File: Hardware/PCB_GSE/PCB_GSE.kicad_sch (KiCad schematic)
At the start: 37 parts, among them J1 Conn_01x06_Pin, U1 STM32F103CBT6

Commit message: wip : Done routing
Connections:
- net 12V_An: now also U1.17 (PA7); no longer U1.14 (PA4)
- net 5V_An: now also U1.18 (PB0); no longer U1.17 (PA7)
- net LCell_An: now also U1.10 (PA0); no longer U1.11 (PA1)
- net Power_Good_12V: now also U1.14 (PA4); no longer U1.15 (PA5)
- net Power_Good_5V: now also U1.15 (PA5); no longer U1.18 (PB0)
- net Pressure_An: now also U1.11 (PA1); no longer U1.10 (PA0)
- net Temp_An: now also U1.13 (PA3); no longer U1.12 (PA2)
- net Valve1_Open: now also U1.31 (PA10); no longer U1.33 (PA12)
- net Valve3_Open: now also U1.33 (PA12); no longer U1.31 (PA10)
- net Vin_An: now also U1.12 (PA2); no longer U1.13 (PA3)

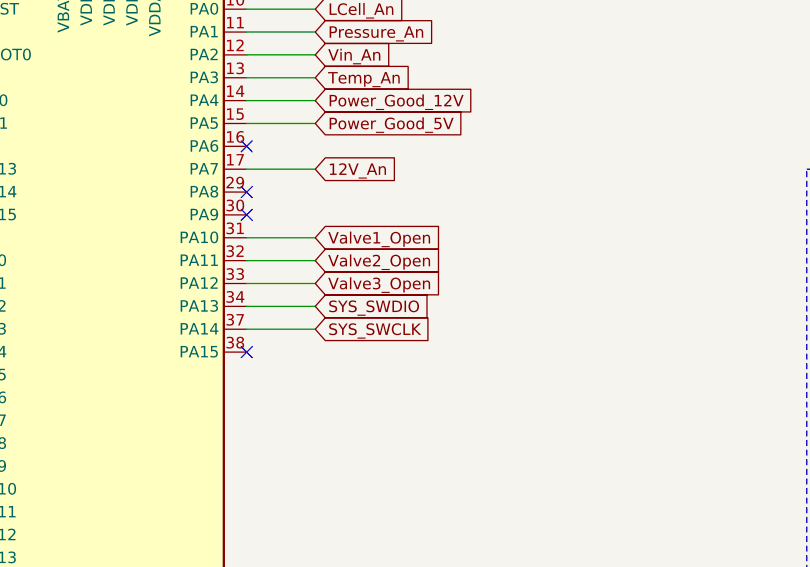
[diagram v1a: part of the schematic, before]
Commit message: fix : replace valve 3 with servomotor on schematic
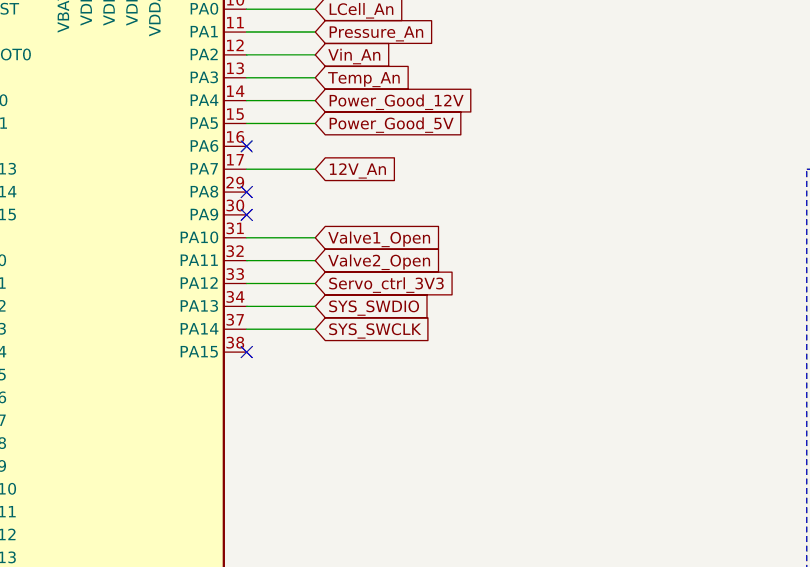
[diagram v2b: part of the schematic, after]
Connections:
- net Valve3_Open renamed Servo_ctrl_3V3
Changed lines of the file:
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@@
 		)
 	)
-	(global_label "Valve3_Open"
+	(global_label "Servo_ctrl_3V3"
 		(shape input)
 		(at 171.45 81.28 0)
@@
 		)
 		(property "Intersheetrefs" "${INTERSHEET_REFS}"
-			(at 186.2884 81.28 0)
+			(at 188.3446 81.28 0)
 			(effects
 				(font

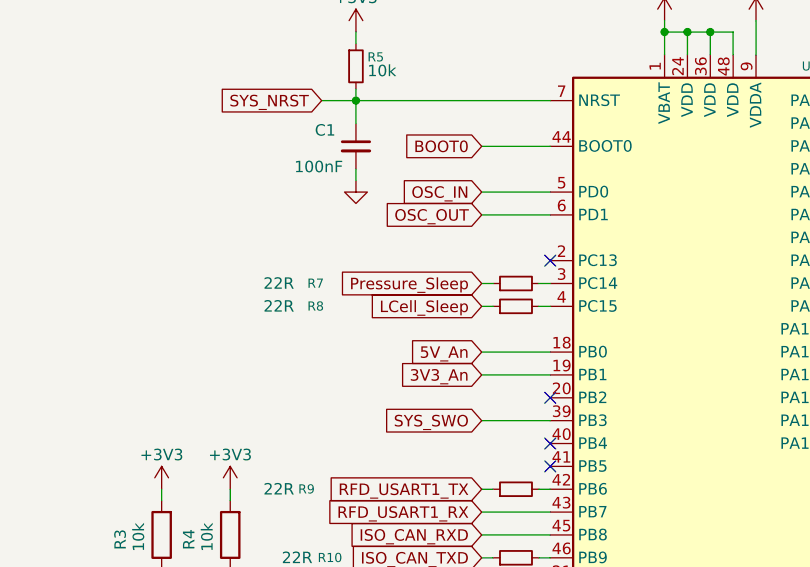
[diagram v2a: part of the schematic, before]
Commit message: fix : replace Pressure sensor amplification circuit with new voltage divider circuit
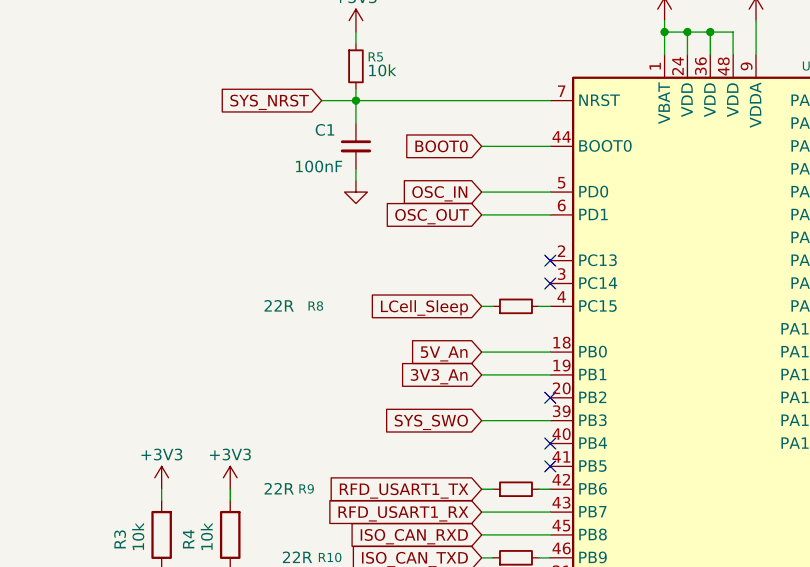
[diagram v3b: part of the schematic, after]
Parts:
- removed R7: 22R, Resistor_SMD:R_0603_1608Metric, symbol Device:R_Small
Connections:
- no-connect marks 10 -> 11
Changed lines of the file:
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@@
+	)
+	(no_connect
+		(at 130.81 71.12)
 	)
 	(no_connect
@@
 	(wire
 		(pts
-			(xy 123.19 71.12) (xy 124.46 71.12)
-		)
-		(stroke
-			(width 0)
-			(type default)
-		)
-	)
-	(wire
-		(pts
 			(xy 205.74 25.4) (xy 208.28 25.4)
 		)
@@
 	(wire
 		(pts
-			(xy 129.54 71.12) (xy 130.81 71.12)
-		)
-		(stroke
-			(width 0)
-			(type default)
-		)
-	)
-	(wire
-		(pts
 			(xy 266.7 34.29) (xy 266.7 36.83)
 		)
@@
 			(width 0)
 			(type default)
-		)
-	)
-	(global_label "Pressure_Sleep"
-		(shape input)
-		(at 123.19 71.12 180)
-		(fields_autoplaced yes)
-		(effects
-			(font
-				(size 1.27 1.27)
-			)
-			(justify right)
-		)
-		(property "Intersheetrefs" "${INTERSHEET_REFS}"
-			(at 105.8115 71.12 0)
-			(effects
-				(font
-					(size 1.27 1.27)
-				)
-				(justify right)
-				(hide yes)
-			)
 		)
 	)
@@
 					(unit 1)
 				)
-			)
-		)
-	)
-	(symbol
-		(lib_id "Device:R_Small")
-		(at 127 71.12 90)
-		(unit 1)
-		(exclude_from_sim no)
-		(in_bom yes)
-		(on_board yes)
-		(dnp no)
-		(property "Reference" "R7"
-			(at 105.664 71.12 90)
-			(effects
-				(font
-					(size 1.016 1.016)
-				)
-				(justify left)
-			)
-		)
-		(property "Value" "22R"
-			(at 102.362 71.12 90)
-			(effects
-				(font
-					(size 1.27 1.27)
-				)
-				(justify left)
-			)
-		)
-		(property "Footprint" "Resistor_SMD:R_0603_1608Metric"
-			(at 127 71.12 0)
-			(effects
-				(font
-					(size 1.27 1.27)
-				)
-				(hide yes)
-			)
-		)
-		(property "Datasheet" "https://www.digikey.ca/en/products/detail/rohm-semiconductor/ESR03EZPJ220/1983463"
-			(at 127 71.12 0)
-			(effects
-				(font
-					(size 1.27 1.27)
-				)
-				(hide yes)
-			)
-		)
-		(property "Description" "Resistor, small symbol"
-			(at 127 71.12 0)
-			(effects
-				(font
-					(size 1.27 1.27)
-				)
-				(hide yes)
-			)
-		)
-		(property "DigiKey_Part_Number" "RHM22DCT-ND"
-			(at 127 71.12 90)
-			(effects
-				(font
-					(size 1.27 1.27)
-				)
-				(hide yes)
-			)
-		)
-		(property "Manufacturer_Part_Number" "ESR03EZPJ220"
-			(at 127 71.12 90)
-			(effects
-				(font
-					(size 1.27 1.27)
-				)
-				(hide yes)
-			)
-		)
-		(pin "1"
-		)
-		(pin "2"
-		)
-		(instances
-			(project "PCB_GSE"
-				(path "/a63f9ed4-21e4-42d0-8bfc-f96143f84d4d"
-					(reference "R7")
-					(unit 1)
-				)

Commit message: fix : done silkscreen and finition
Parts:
- renumbered C2 to C13, C5 to C14, C7 to C15, C11 to C16, C10 to C18, C4 to C19, C1 to C20, C6 to C22, C9 to C24, C8 to C26, C3 to C28, LED1 to D4, FB1 to FB2, H2 to H1, H1 to H2, J1 to J4, R8 to R10, R5 to R17, R1 to R21, R2 to R22, R3 to R23, R4 to R24, R11 to R6, R10 to R7, R9 to R8, R12 to R9, U1 to U5, XTAL-1 to Y1

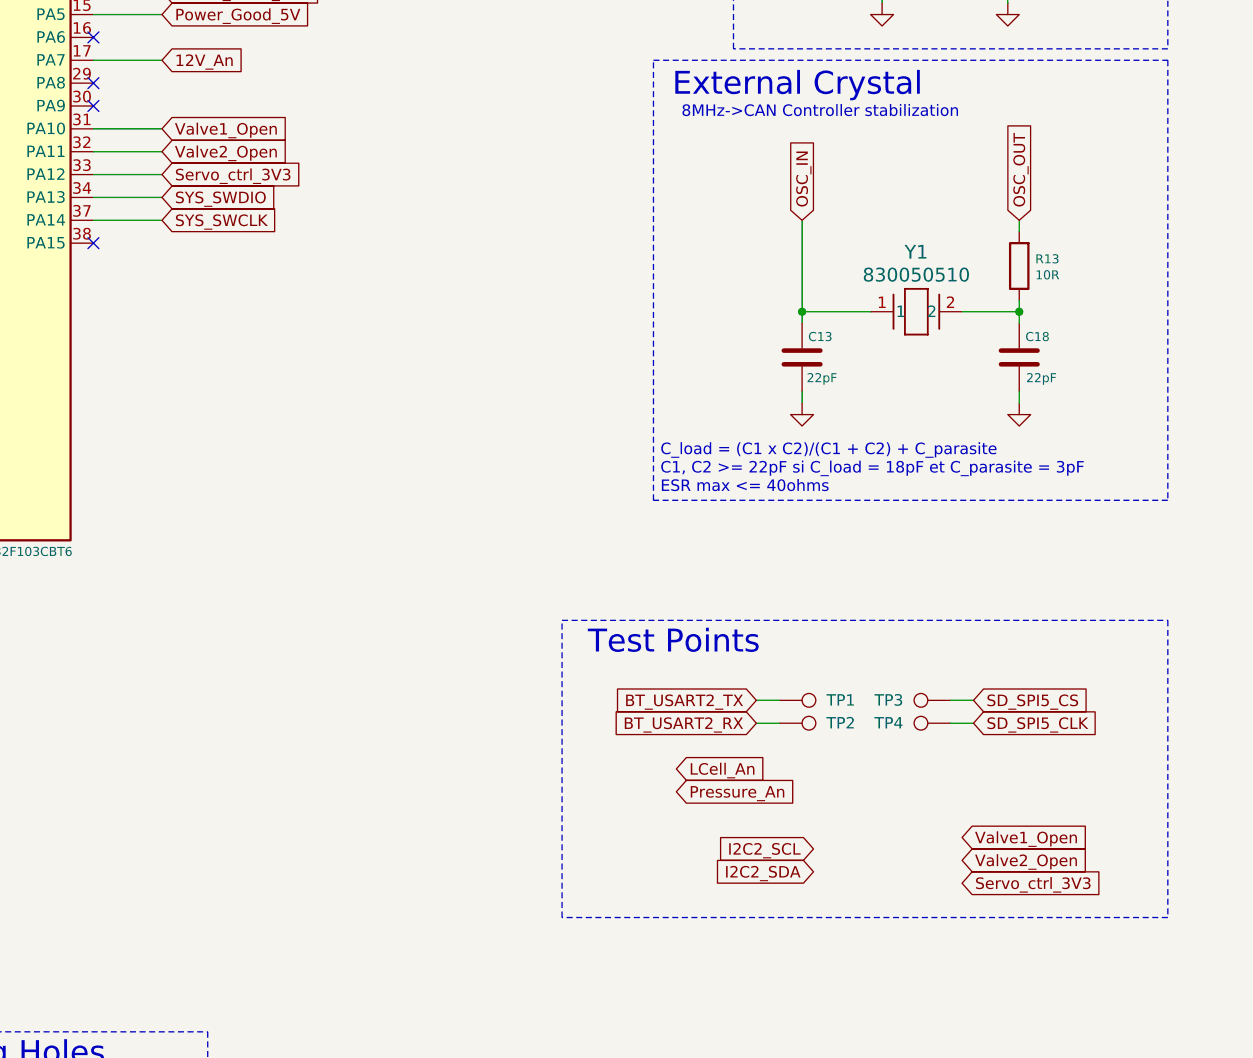
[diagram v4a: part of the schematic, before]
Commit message: fix(gse): Vin servo
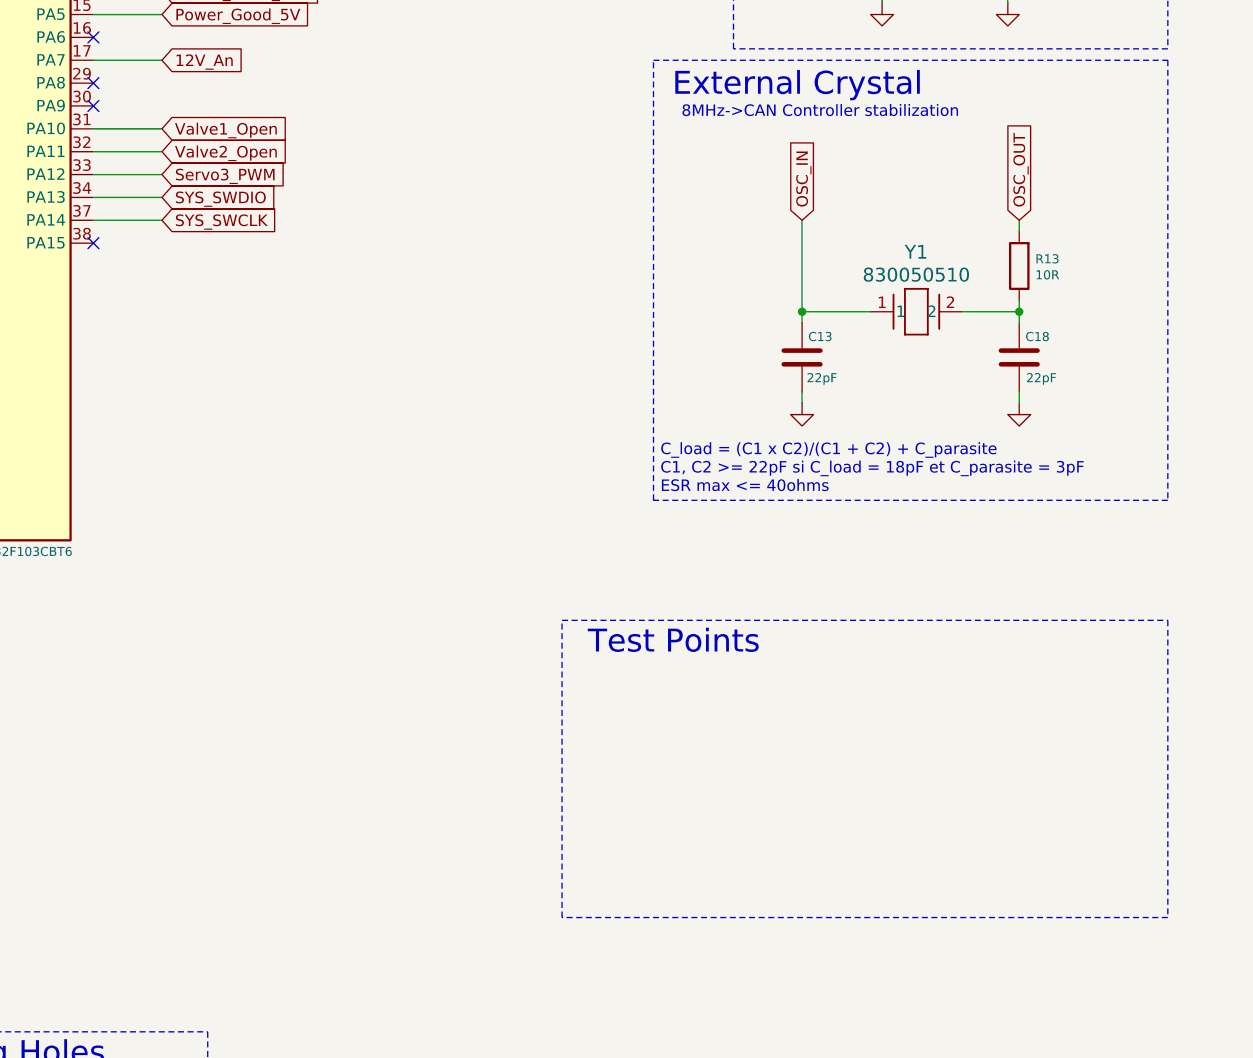
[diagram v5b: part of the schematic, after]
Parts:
- removed TP1, TP2, TP3, TP4: TestPoint, TestPoint:TestPoint_Pad_D1.0mm, symbol Connector:TestPoint
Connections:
- net Servo_ctrl_3V3 renamed Servo3_PWM

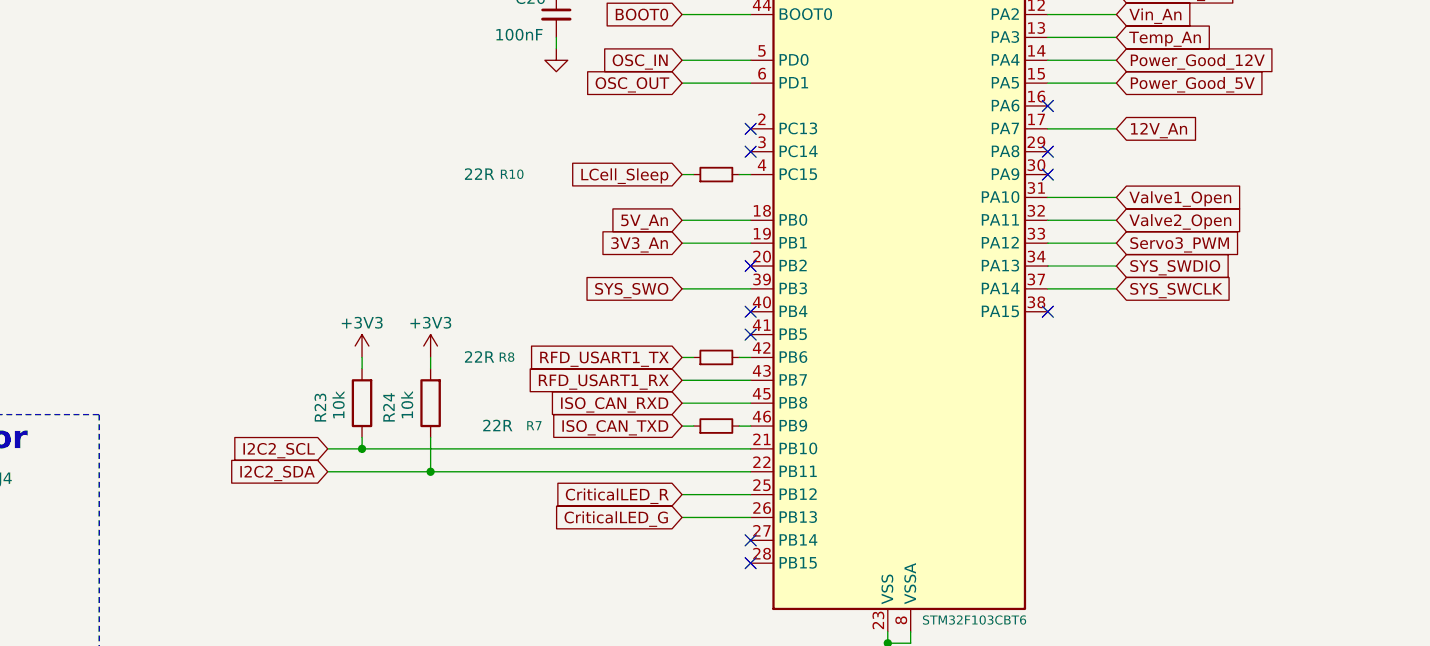
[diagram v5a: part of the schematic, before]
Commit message: fix(gse): change Servo3_PWM -> TIM1_CH2, change Valve1/2_Open pin
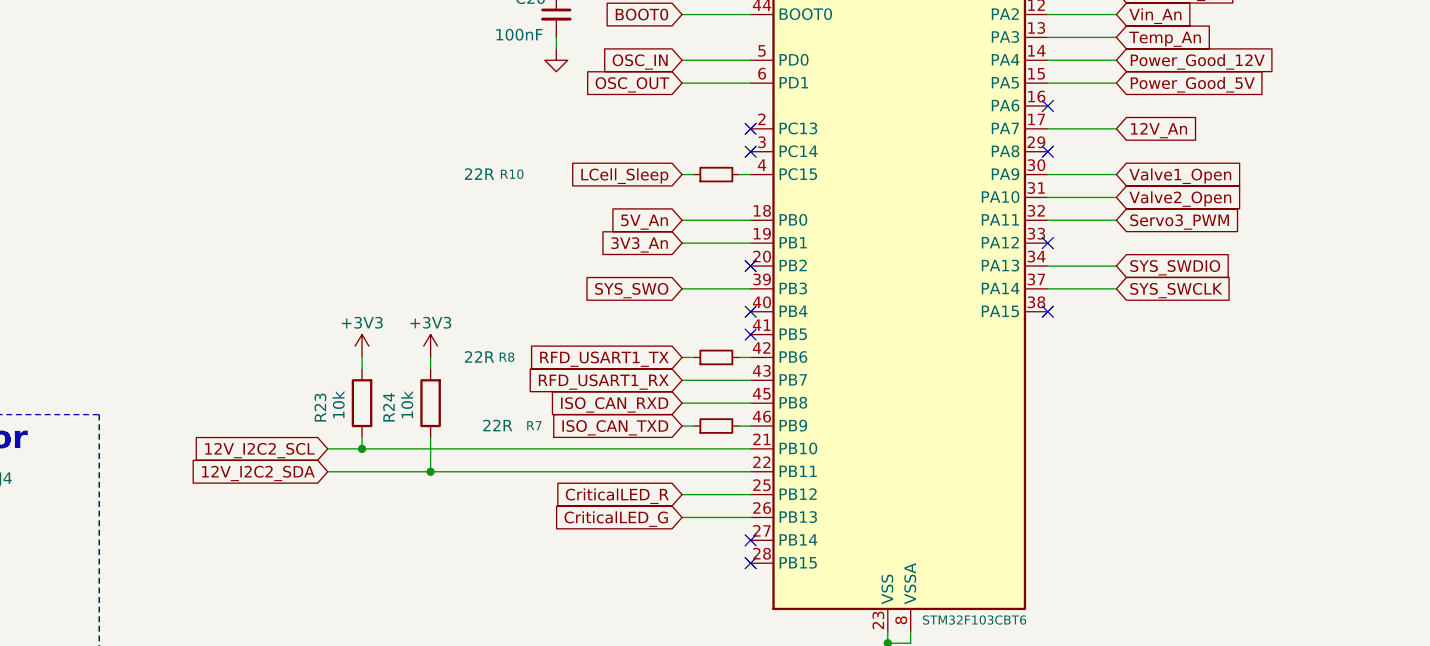
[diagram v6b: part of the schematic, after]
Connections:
- net Servo3_PWM: now also U5.32 (PA11); no longer U5.33 (PA12)
- net Valve1_Open: now also U5.30 (PA9); no longer U5.31 (PA10)
- net Valve2_Open: now also U5.31 (PA10); no longer U5.32 (PA11)
- net I2C2_SCL renamed 12V_I2C2_SCL
- net I2C2_SDA renamed 12V_I2C2_SDA
